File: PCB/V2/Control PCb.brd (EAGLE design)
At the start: 48.9 x 83.8 mm, 31 parts, among them Q1 DMP2305U-7, Q2 BSS123, Q3 BSS123, U1 V_REG_317DPACK, U2 5ACFEW

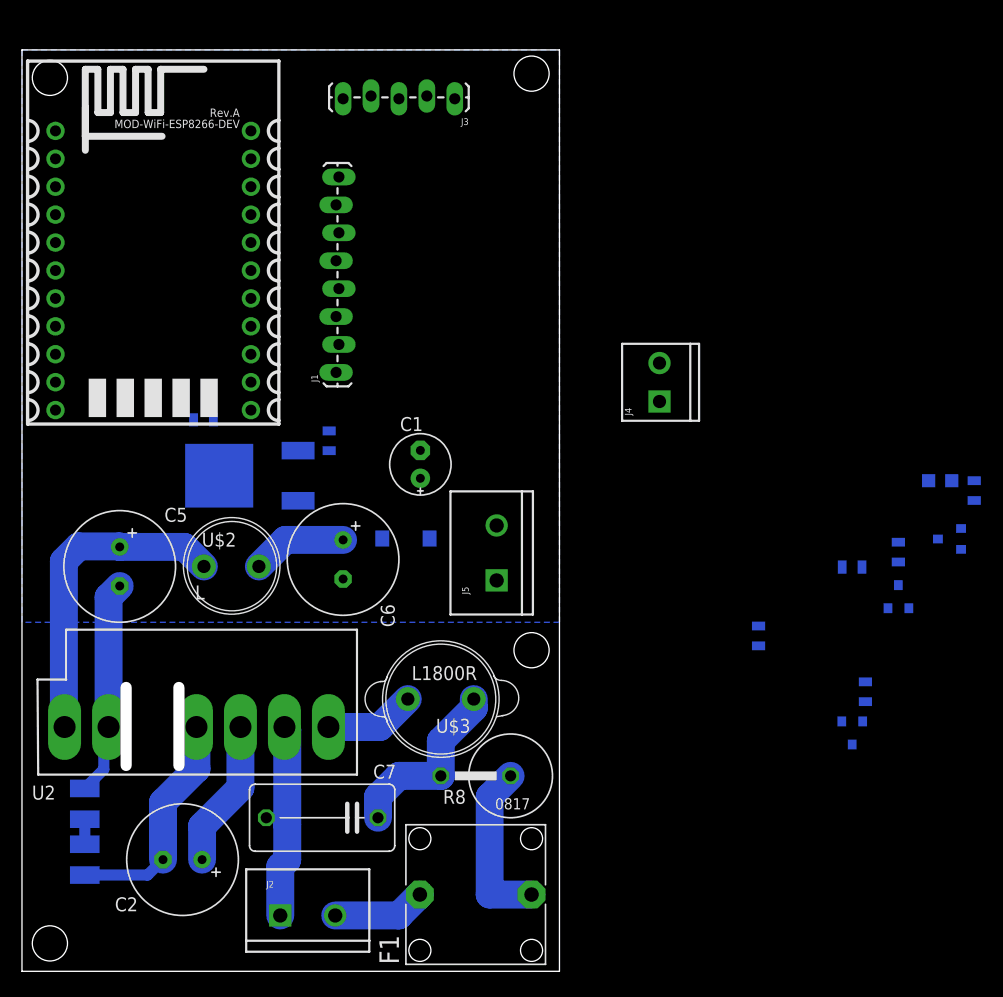
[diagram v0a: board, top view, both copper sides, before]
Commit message: PCB + ArduinoOTA working
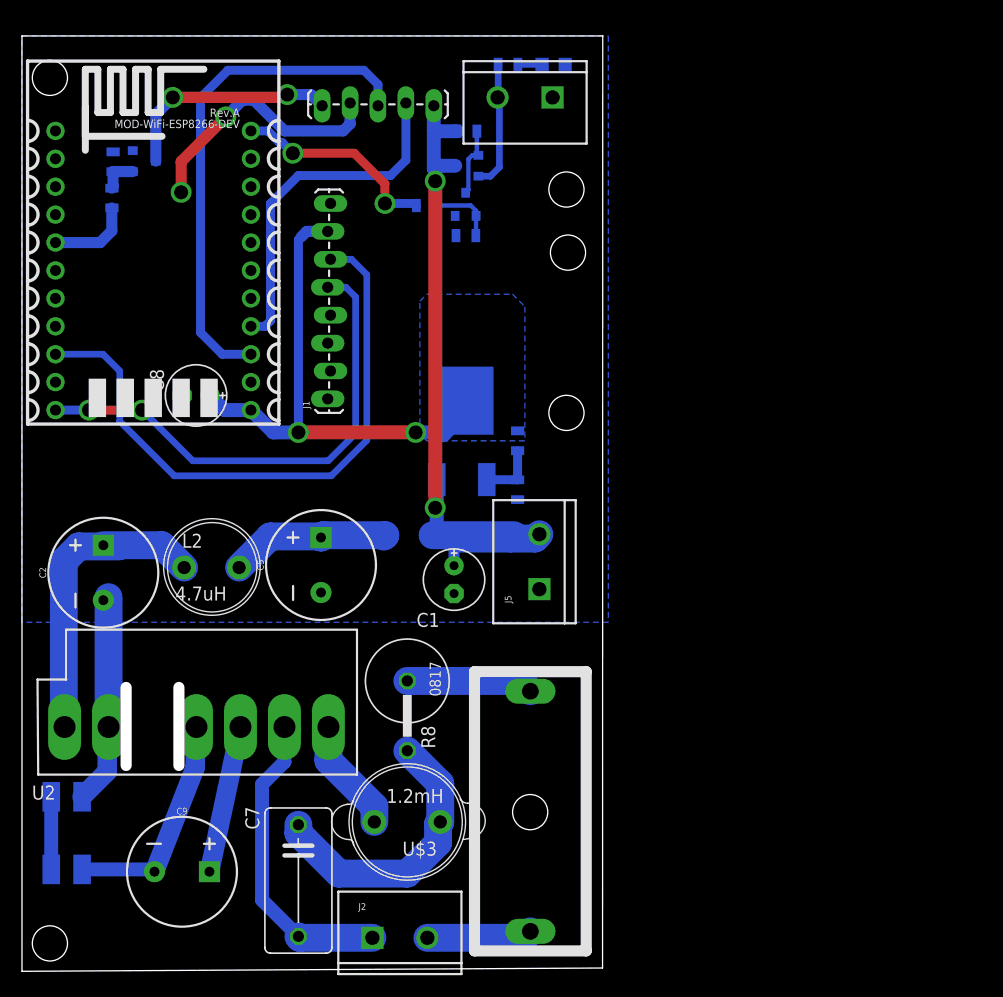
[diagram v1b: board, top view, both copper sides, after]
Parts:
- removed C6: (no value), adafruit:E3,5-10
- removed J4: (no value), SparkFun-Connectors:SCREWTERMINAL-3.5MM-2
- removed R5: 0, RJC-2:0805
- removed U$2: L, adafruit:6000
- added C8: (no value), adafruit:E2,5-6E
- added C9: 10uF, SparkFun-Capacitors:CPOL-RADIAL-5MM-10MM-KIT
- added J6: (no value), SparkFun-Connectors:SCREWTERMINAL-5MM-2
- added L2: 4.7uH, adafruit:6000
- added R10, R9: 0, RJC-2:0805
- C2: value (none) -> 470; device adafruit:E3,5-10 -> SparkFun-Capacitors:CPOL-RADIAL-5MM-10MM-KIT
- C5: value (none) -> 100; device adafruit:E3,5-10 -> SparkFun-Capacitors:CPOL-RADIAL-5MM-10MM-KIT
- C7: value (none) -> 0.1uF
- F1: value (none) -> 4527; device fuse:F456 -> RJC-2:4527
- R8: value (none) -> 12/3W
- U$3: value L1800R -> 1.2mH
- moved Q3 82.8 mm to (11.1, 63.5), turned to 90 degrees
- moved R4 71.0 mm to (8.18, 60.2), turned to 90 degrees
- moved R3 57.5 mm to (44.2, 72.3), turned to 0 degrees
- moved Q1 55.5 mm to (40.5, 63.1)
- moved R2 54.8 mm to (40.5, 66.3), turned to 0 degrees
- moved Q2 53.1 mm to (40.4, 59.6)
- moved D1 51.7 mm to (48.4, 72.3), turned to 90 degrees
- moved R1 50.8 mm to (36.8, 59.5)
- moved R7 28.6 mm to (45.1, 38.1), turned to 90 degrees
- moved C2 27.1 mm to (7.40, 26.1), turned to 90 degrees
- moved U1 20.2 mm to (40.0, 39.4), turned to 0 degrees
- moved C5 18.3 mm to (27.2, 26.8), turned to 90 degrees
- moved R6 17.7 mm to (45.1, 33.7), turned to 90 degrees
- moved U$3 11.6 mm to (35.1, 3.43)
- moved C1 10.9 mm to (39.3, 25.5), turned to 270 degrees
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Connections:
- removed net 3.3V: U$1.1
- new net IO12: R4.1, U$1.16
- new net SCL: J1.5, U$1.22
- new net SDA: J1.6, U$1.20
- net +3V3: now also C8.+, J1.7, U$1.1
- net GND: now also C2.-, C8.-, J1.8, J6.1, R10.1, R9.1; no longer C6.-, J4.2
- net N$1: now also D1.A, R3.1; no longer R1.1
- net N$13: now also C9.+; no longer C2.+
- net N$14: now also C9.-; no longer C2.-
- net N$17: now also C2.+, L2.1; no longer C5.+, U$2.1
- net N$18: now also C5.+, L2.2; no longer C6.+, U$2.2
- net N$2: now also R9.2
- net N$6: now also J6.2, R3.2; no longer J4.1, R3.1
- net N$7: now also R1.1, U$1.11; no longer D1.A, R3.2
- net N$8: now also R10.2; no longer R5.2
- net RX: now also U$1.3
- net TX: now also U$1.4
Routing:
- net +5V: track 0.00 -> 63.9 mm, vias 0 -> 2
- net SDA: track 0.00 -> 55.9 mm
- net +3V3: track 0.00 -> 47.4 mm, vias 0 -> 2
- net RX: track 0.00 -> 46.4 mm
- net SCL: track 0.00 -> 45.6 mm, vias 0 -> 2
- net TX: track 0.00 -> 31.8 mm
- net GND: track 19.5 -> 43.4 mm, vias 0 -> 2
- net DISPLAY_RESET: track 0.00 -> 20.5 mm, vias 0 -> 2
- net N$7: track 0.00 -> 19.1 mm, vias 0 -> 2
- net N$6: track 0.00 -> 11.7 mm
- net N$11: track 16.6 -> 25.9 mm
- net N$4: track 19.7 -> 28.6 mm
- net IO12: track 0.00 -> 7.66 mm
- net N$5: track 0.00 -> 6.47 mm
- net N$18: track 8.66 -> 14.8 mm
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- added copper zone on layer 16, net +3V3
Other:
- board size 48.9 x 83.8 mm -> 52.8 x 85.1 mm

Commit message: Code + PCB stuff
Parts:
- removed J6: (no value), SparkFun-Connectors:SCREWTERMINAL-5MM-2
- added D3: LED_GREEN, RJC-2:CHIP_LED0805
- added J4: (no value), SparkFun-Connectors:SCREWTERMINAL-5MM-3
- added Q4: DMP2305U-7, RJC-2:SOT23
- added Q5: BSS123, RJC-2:SOT23
- added R11, R12, R13, R5: 0, RJC-2:0805
- moved U$3 10.1 mm to (36.4, 13.5), turned to 90 degrees
- moved D1 9.65 mm to (38.7, 73.0), turned to 270 degrees
- moved R8 7.96 mm to (32.8, 3.56), turned to 180 degrees
- moved R2 5.96 mm to (42.7, 60.7), turned to 180 degrees
- moved R7 3.86 mm to (48.9, 37.5)
- moved J1 3.86 mm to (31.8, 41.3)
- moved U1 3.86 mm to (43.8, 38.7)
- moved R6 3.81 mm to (48.9, 33.7)
- moved Q2 2.69 mm to (42.3, 57.7)
- moved R9 2.52 mm to (42.0, 54.9)
- moved J2 2.40 mm to (33.9, -5.84)
- moved C7 2.30 mm to (27.4, -1.65)
- moved Q1 2.07 mm to (42.5, 63.5), turned to 90 degrees
- moved R3 1.80 mm to (42.5, 73.0), turned to 180 degrees
- moved R1 1.80 mm to (38.1, 58.2)
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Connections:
- new net N$16: J4.3, Q4.2, R5.2
- new net N$19: D3.A, R5.1
- new net N$20: Q4.1, Q5.3, R11.1
- new net N$21: R13.1, U$1.18
- new net N$22: Q5.1, R12.2, R13.2
- net +5V: now also Q4.3, R11.2
- net GND: now also D3.C, J4.2, Q5.2, R12.1; no longer J6.1
- net N$6: now also J4.1; no longer J6.2
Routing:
- net GND: track 43.4 -> 21.1 mm, vias 2 -> 0
- net N$7: track 19.1 -> 0.00 mm, vias 2 -> 0
- net RX: track 46.4 -> 32.1 mm
- net N$16: track 0.00 -> 14.1 mm
- net N$11: track 25.9 -> 13.1 mm
- net +5V: track 63.9 -> 74.9 mm, vias 2 -> 3
- net N$10: track 11.6 -> 20.0 mm
- net N$20: track 0.00 -> 6.68 mm
- net +3V3: track 47.4 -> 53.6 mm
- net SDA: track 55.9 -> 60.7 mm
- net N$22: track 0.00 -> 4.16 mm
- net SCL: track 45.6 -> 49.1 mm
- net N$5: track 6.47 -> 4.09 mm
- net N$6: track 11.7 -> 9.67 mm
- net N$19: track 0.00 -> 1.86 mm
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- added copper zone on layer 16, net +5V
- added copper zone on layer 16, net N$21
- added copper zone on layer 16, net N$7
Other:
- board size 52.8 x 85.1 mm -> 57.1 x 86.4 mm
